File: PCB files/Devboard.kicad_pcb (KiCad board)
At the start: 2 copper layers, 42.1 x 52.1 mm, 41 parts, among them IC1 MPU-6500, J1 USB_C_Receptacle_USB2.0_14P, J2 Conn_01x03, J3 Conn_01x20, J4 Conn_01x20, J5 JST_2mm_LiPo, SW1 SW_Push, U1 RP2040, U2 NCP1117-3.3_SOT223, U3 W25Q128JVS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

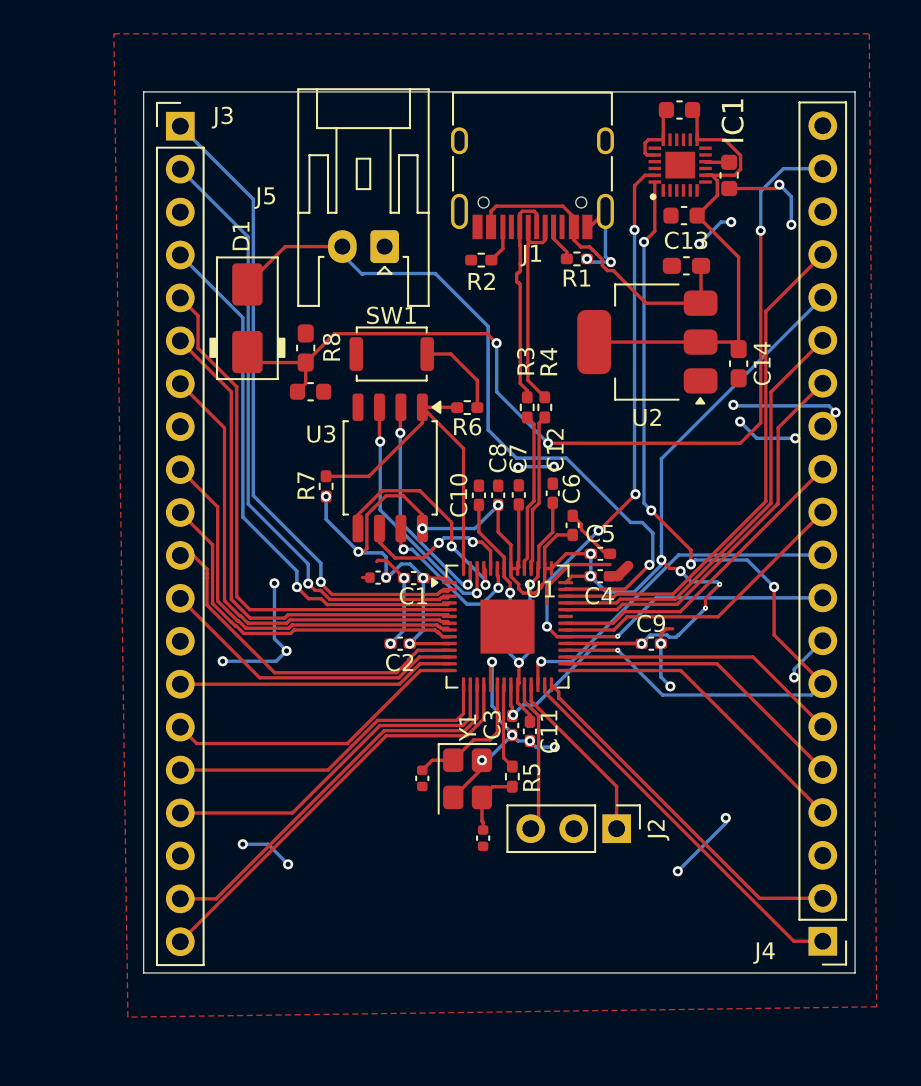
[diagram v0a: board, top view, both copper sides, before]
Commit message: added rounded corners and also added silkscreen text
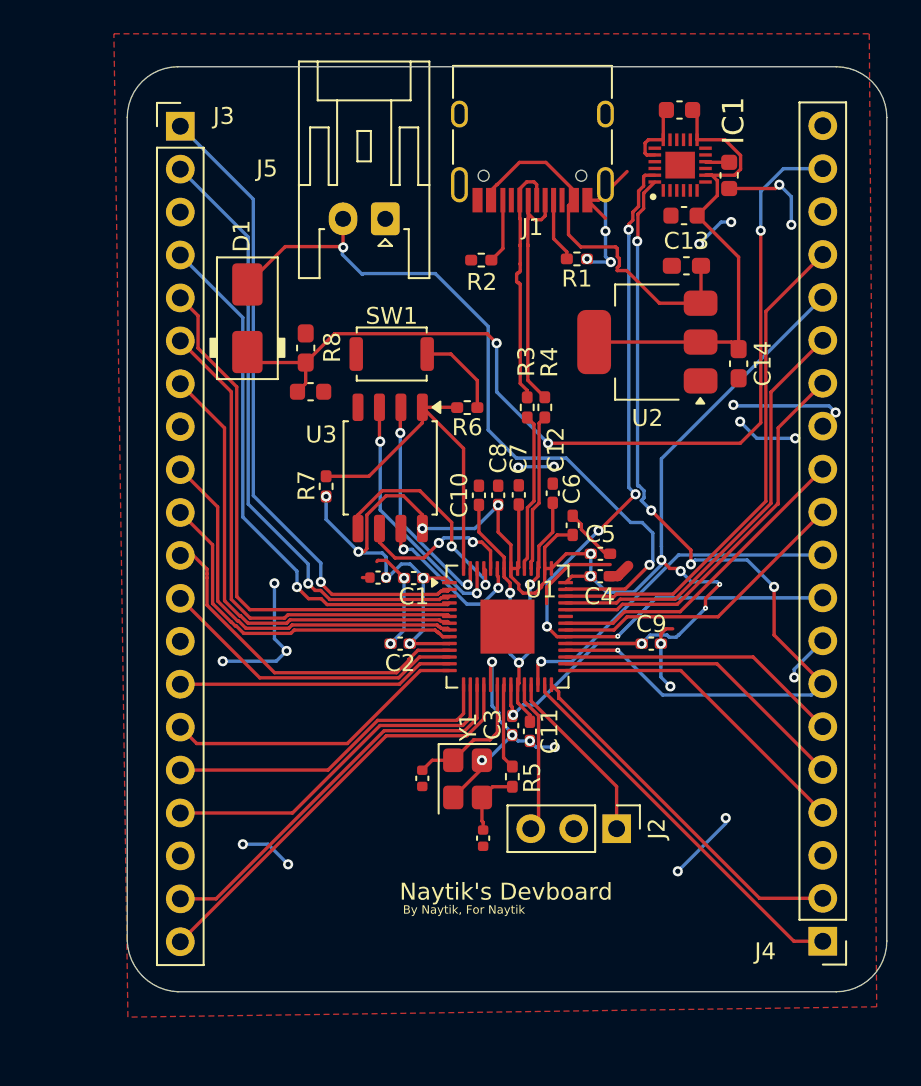
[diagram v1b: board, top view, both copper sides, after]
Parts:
- moved J5 1.64 mm to (192.0, 69.3)
- moved J1 1.58 mm to (200.7, 64.2)
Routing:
- net GND: track 84.5 -> 89.3 mm, vias 29 -> 30
- net Net-(U2-VI): track 19.1 -> 22.2 mm
- net USB_D-: track 13.2 -> 15.1 mm
- net USB_D+: track 13.2 -> 14.9 mm
- net /GPIO29_ADC3: track 43.4 -> 45.1 mm, vias 1 -> 2
- net Net-(J1-CC1): track 2.22 -> 3.80 mm
- net Net-(J1-CC2): track 2.25 -> 3.17 mm
- net /GPIO21: track 53.2 -> 53.8 mm
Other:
- board size 42.1 x 52.1 mm -> 44.9 x 54.7 mm
- board text added: "By Naytik, For Naytik"
- board text added: "Naytik's Devboard"

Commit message: changes for rounded corners!
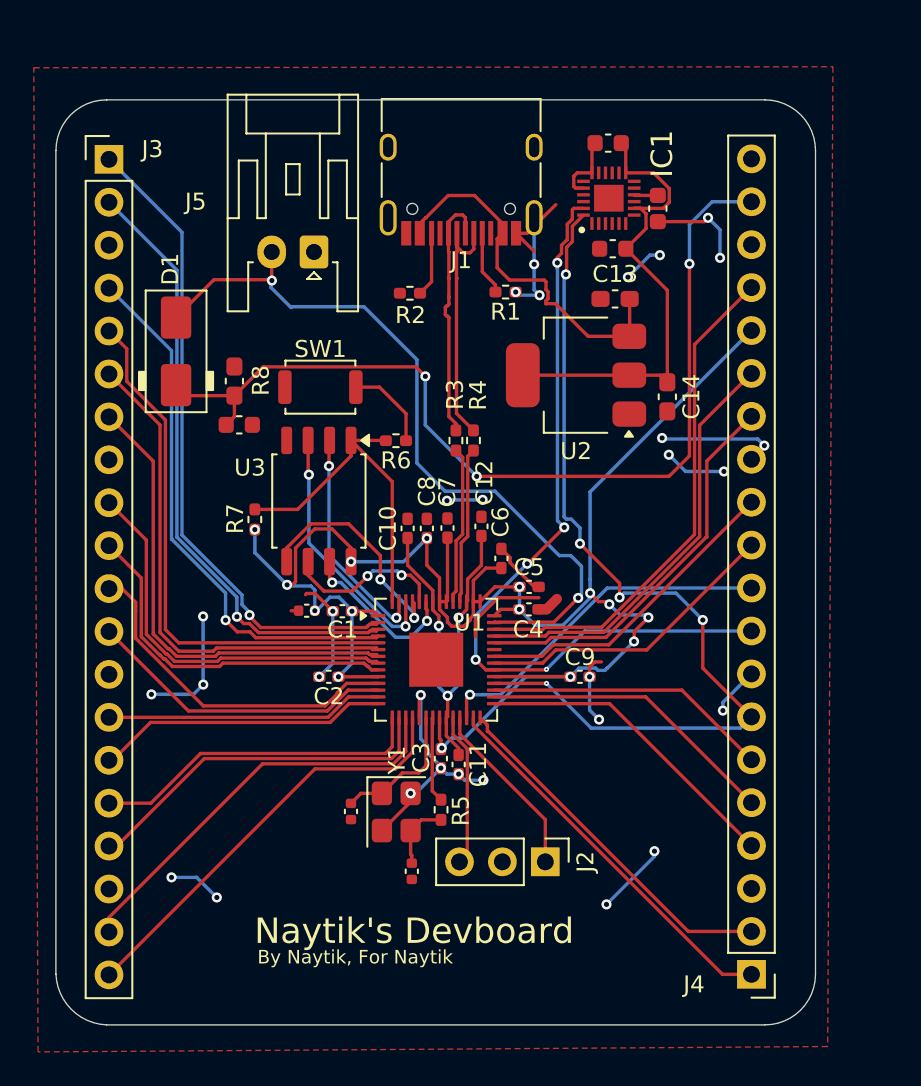
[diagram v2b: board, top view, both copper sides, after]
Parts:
- moved C7 4.65 mm to (195.6, 87.7)
- moved R3 4.65 mm to (196.1, 82.5)
- moved C10 4.65 mm to (193.3, 87.7)
- moved C13 4.65 mm to (205.6, 74.1)
- moved C15 4.65 mm to (189.9, 104.4)
- moved C17 4.65 mm to (187.3, 92.5)
- moved C18 4.65 mm to (183.3, 81.5)
- moved C19 4.65 mm to (205.2, 64.9)
- moved C2 4.65 mm to (188.6, 96.5)
- moved C21 4.65 mm to (205.4, 71.1)
- moved C3 4.65 mm to (195.2, 101.3)
- moved C6 4.65 mm to (198.8, 89.5)
- moved C8 4.65 mm to (194.4, 87.7)
- moved C9 4.65 mm to (203.5, 96.5)
- moved J2 4.65 mm to (201.4, 107.4)
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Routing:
- net GND: track 89.3 -> 88.2 mm
- net /GPIO11: track 18.1 -> 17.2 mm
- net /GPIO14: track 24.0 -> 24.5 mm
